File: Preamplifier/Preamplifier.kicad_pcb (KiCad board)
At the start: 2 copper layers, 100 x 58 mm, 64 parts, among them J1 POWER, J2 IN_L, J3 IN_R, J4 OUT_L, J5 OUT_R, U1 OPA1612AxD, U2 OPA1612AxD, U3 OPA1612AxD, U4 OPA1612AxD

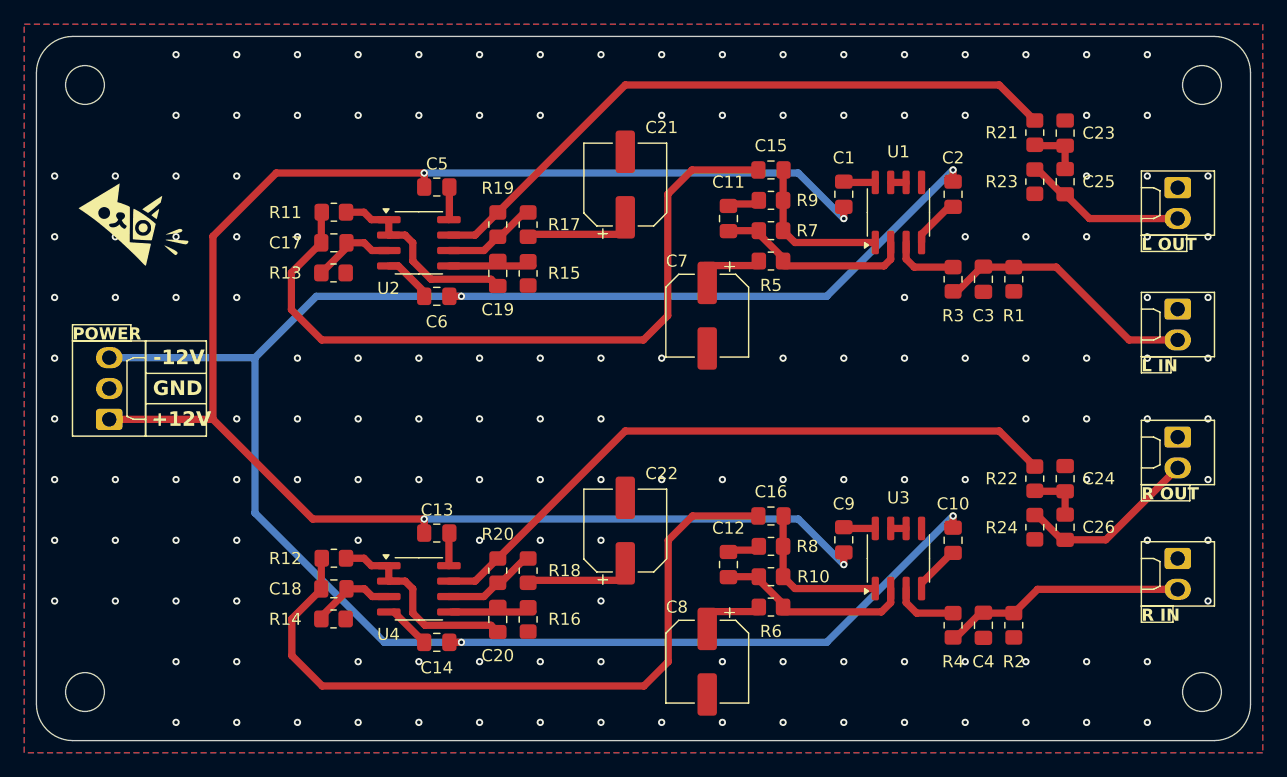
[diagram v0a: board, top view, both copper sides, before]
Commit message: Board Designs
Updated the power supply board design.
Updated the preamplifier board design.
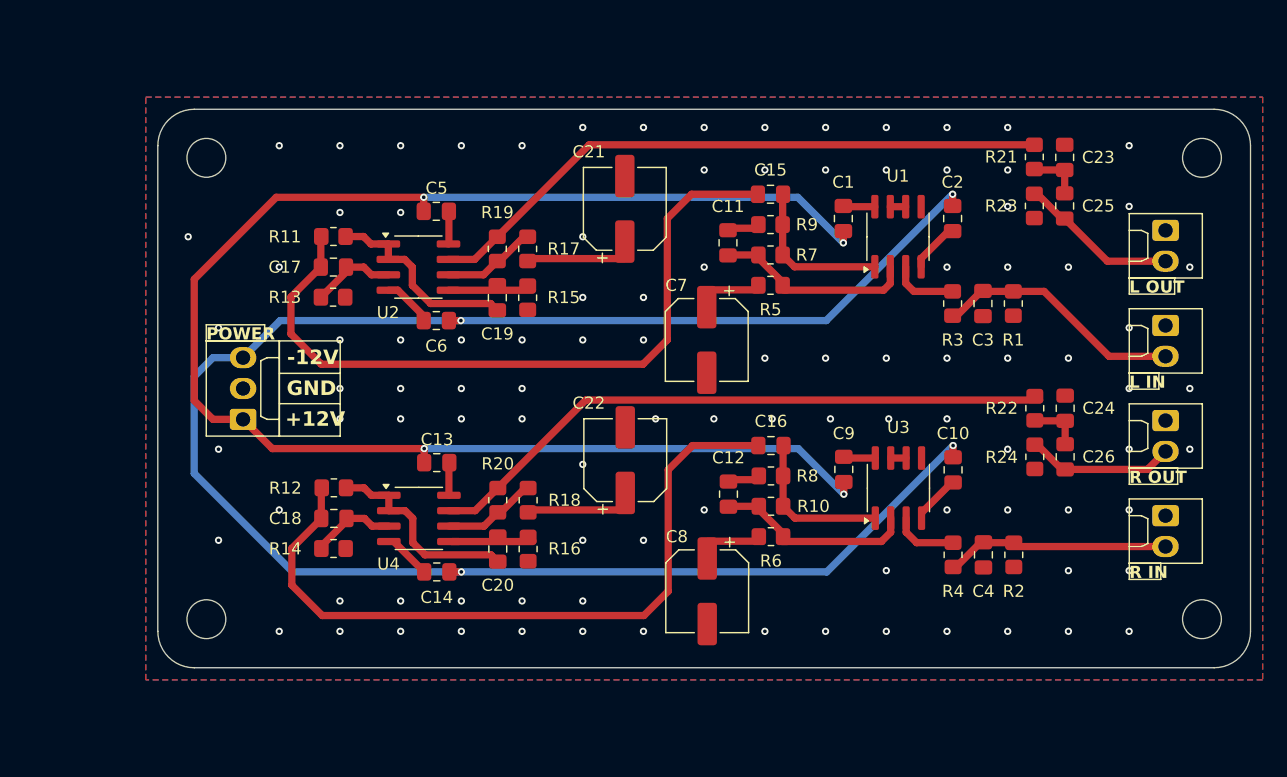
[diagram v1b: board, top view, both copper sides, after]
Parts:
- removed the G*** at (104.0, 86.5)
- added G***: LOGO, Logos:PhonoPreamp, B.Cu at (145.8, 100.0)
- moved H1 11.7 mm to (110.0, 81.0)
- moved H3 11.7 mm to (110.0, 119.0)
- moved J1 11.0 mm to (113.0, 102.5)
- moved H2 6.00 mm to (192.0, 81.0)
- moved H4 6.00 mm to (192.0, 119.0)
- moved C9 5.80 mm to (162.5, 106.7)
- moved C10 5.80 mm to (171.5, 106.7)
- moved C12 5.80 mm to (153.0, 108.7)
- moved C13 5.80 mm to (129.0, 106.1)
- moved C14 5.80 mm to (129.0, 115.1)
- moved C16 5.80 mm to (156.5, 104.7)
- moved C18 5.80 mm to (120.5, 110.7)
- moved C20 5.80 mm to (134.0, 113.2)
- moved C22 5.80 mm to (144.5, 105.9)
- moved C24 5.80 mm to (180.7, 101.6)
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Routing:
- net +12V: track 140.5 -> 128.8 mm
- net -12V: track 158.8 -> 150.7 mm
- net Net-(J5-Pin_2): track 14.6 -> 11.8 mm
- net Net-(R19-Pad2): track 54.6 -> 52.2 mm
- net Net-(R20-Pad2): track 54.6 -> 52.4 mm
- net Net-(J3-Pin_2): track 19.7 -> 18.2 mm
- net Net-(J2-Pin_2): track 21.3 -> 20.1 mm
- net GND: vias 150 -> 100
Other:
- board size 100 x 58 mm -> 90 x 46 mm

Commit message: Board Designs
Updated the power supply board design.
Updated the preamplifier board design.
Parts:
- added G***: LOGO, Logos:Cat, F.Cu at (121.5, 82.0)

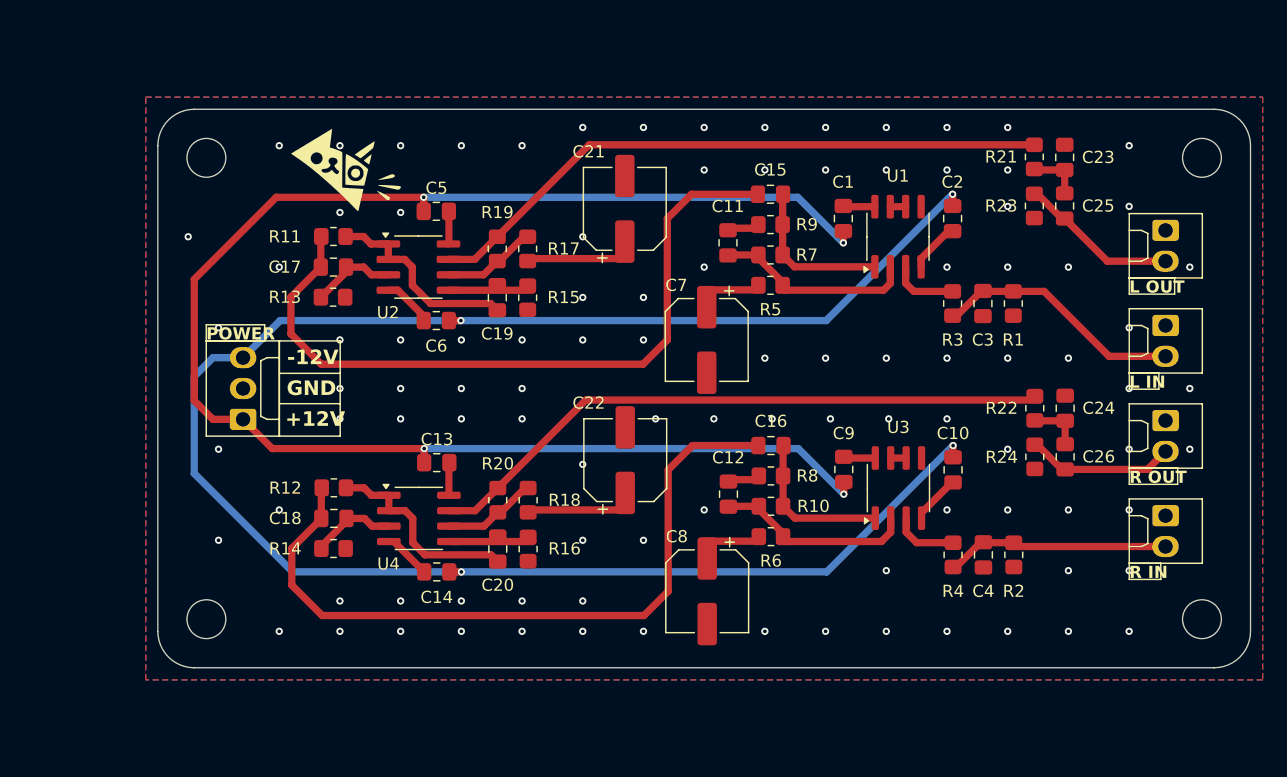
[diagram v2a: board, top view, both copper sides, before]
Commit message: Preamplifier Board
Updated the preamplifier schematic.
Updated the preamplifier board design.
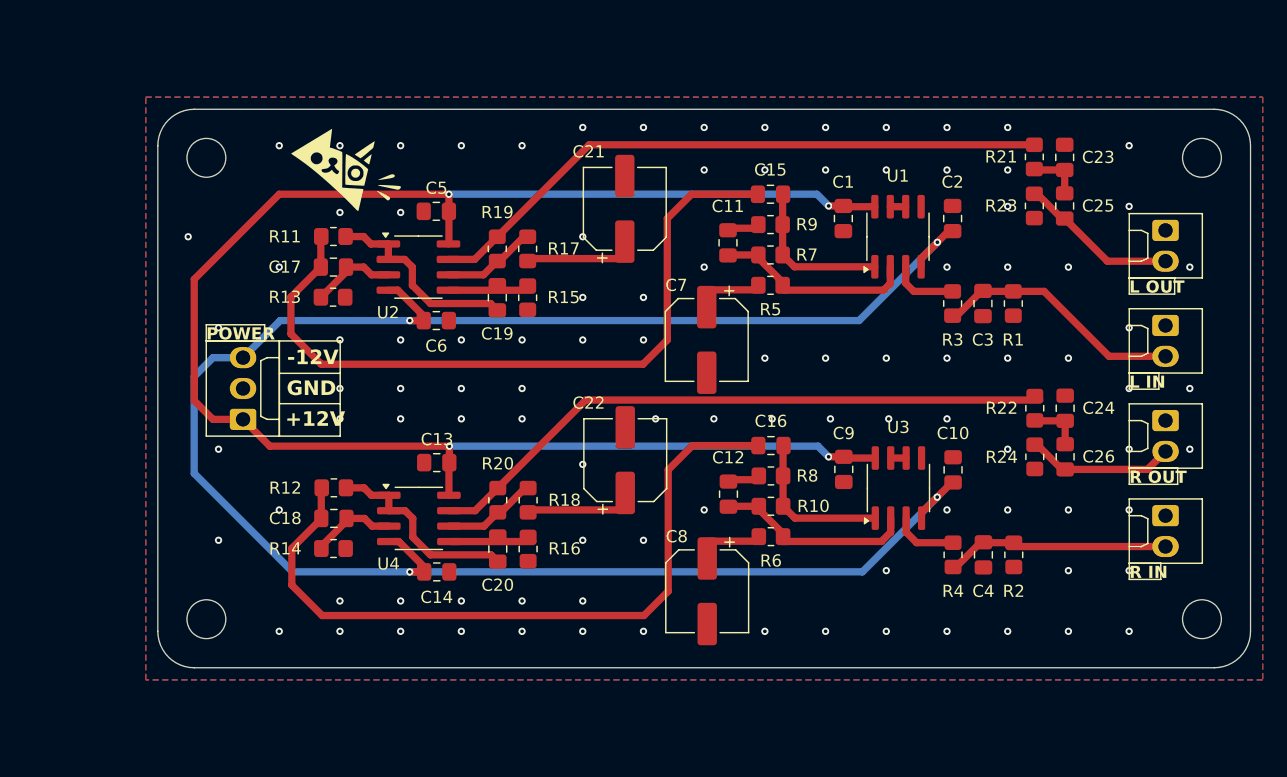
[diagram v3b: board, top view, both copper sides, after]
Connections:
- C1 pad 1: +12V -> GND
- C1 pad 2: Net-(U1C-V+) -> +12V
- C10 pad 1: Net-(U3C-V-) -> -12V
- C10 pad 2: -12V -> GND
- C13 pad 1: +12V -> GND
- C13 pad 2: Net-(U4C-V+) -> +12V
- C14 pad 1: Net-(U4C-V-) -> -12V
- C14 pad 2: -12V -> GND
- C2 pad 1: Net-(U1C-V-) -> -12V
- C2 pad 2: -12V -> GND
- C5 pad 1: +12V -> GND
- C5 pad 2: Net-(U2C-V+) -> +12V
- C6 pad 1: Net-(U2C-V-) -> -12V
- C6 pad 2: -12V -> GND
- C9 pad 1: +12V -> GND
- C9 pad 2: Net-(U3C-V+) -> +12V
- U1 pad 4: Net-(U1C-V-) -> -12V
- U1 pad 8: Net-(U1C-V+) -> +12V
- U2 pad 4: Net-(U2C-V-) -> -12V
- U2 pad 8: Net-(U2C-V+) -> +12V
- U3 pad 4: Net-(U3C-V-) -> -12V
- U3 pad 8: Net-(U3C-V+) -> +12V
- U4 pad 4: Net-(U4C-V-) -> -12V
- U4 pad 8: Net-(U4C-V+) -> +12V
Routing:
- net -12V: track 150.7 -> 158.3 mm
- net +12V: track 128.8 -> 135.3 mm
- net Net-(U1C-V-): track 3.87 -> 0.00 mm
- net Net-(U2C-V-): track 3.79 -> 0.00 mm
- net Net-(U4C-V-): track 3.54 -> 0.00 mm
- net Net-(U3C-V-): track 3.53 -> 0.00 mm
- net Net-(U2C-V+): track 2.71 -> 0.00 mm
- net Net-(U4C-V+): track 2.65 -> 0.00 mm
- net Net-(U1C-V+): track 2.53 -> 0.00 mm
- net Net-(U3C-V+): track 2.50 -> 0.00 mm
